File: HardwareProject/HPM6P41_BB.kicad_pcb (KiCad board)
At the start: 4 copper layers, 100 x 80.3 mm, 276 parts, among them J1 排针, J10 Conn_01x01, J11 Conn_01x01, J12 Conn_01x01, J13 排针, J14 排针, J2 USB_C_Receptacle_USB2.0_16P, J4 Conn_ARM_JTAG_SWD_20, J5 Conn_01x03, J6 Conn_01x03, J7 SMA, J8 SMA, J9 Conn_01x01, Q1 HYG080N10LS1C2, Q2 HYG080N10LS1C2, Q3 HYG080N10LS1C2, Q4 HYG080N10LS1C2, Q5 S8050, Q7 S8050, SW1 焊盘, SW2 Push_Button, SW3 Push_Button, SW4 Push_Button, U1 UCC27211ADRMR, U10 TJA1044GTK/3Z, U11 TPS54302, U12 LP5907MFX-3.3, U13 REF3030, U14 LM5164DDA, U15 SY8089, U16 INA241A3xDDF, U18 UCC27517, U2 UCC27211ADRMR, U20 SGM8551XN, U21 SGM8551XN, U22 TMP112xxDRL, U23 TPD4E05U06DQA, U24 CA-IS3762HN, U25 SYR838, U26 XC6206PxxxMR, U27 CA-IS3762HN, U28 TME-0505S, U3 UCC27517, U4 HPM6P41IPB1, U5 TPD4E05U06DQA, U6 AT24C08C-SSHM-T, U7 TMP112xxDRL, U8 TMP112xxDRL, U9 SIT3088ETK, Y1 24MHz ±10ppm 6pF

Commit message: 完成Rev4 电源 驱动 模拟 IO
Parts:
- removed R57: 1kΩ, Resistor_SMD:R_0603_1608Metric
- removed R75: 33Ω, Resistor_SMD:R_0603_1608Metric
- removed U21: SGM8551XN, Package_TO_SOT_SMD:TSOT-23-5
- added C104: SCC2211X102K502TG, kicad_community_lib:SCC2211X102K502T, F.Cu at (99.2, 123.5)
- added C105: SCC2211X102K502TG, kicad_community_lib:SCC2211X102K502T, B.Cu at (96.4, 102.9)
- added C98: 47pF,50V, Capacitor_SMD:C_0603_1608Metric, F.Cu at (184.2, 70.7)
- added R17: 10K, Resistor_SMD:R_0603_1608Metric, F.Cu at (129.2, 107.6)
- added R25: 10K, Resistor_SMD:R_0603_1608Metric, F.Cu at (129.2, 106.1)
- added R26: 10K, Resistor_SMD:R_0603_1608Metric, F.Cu at (143.2, 106.9)
- added R27: 100Ω, Resistor_SMD:R_0603_1608Metric, F.Cu at (185.0, 68.4)
- added R28: 100Ω, Resistor_SMD:R_0603_1608Metric, F.Cu at (183.5, 68.5)
- added R32: 1kΩ, Resistor_SMD:R_0603_1608Metric, F.Cu at (146.6, 76.6)
- added TP5: TestPoint_Probe, HPM6P41_BB:测试点, F.Cu at (126.1, 71.1)
- added TP6: TestPoint_Probe, HPM6P41_BB:测试点, F.Cu at (123.1, 71.1)
- added TP8: TestPoint_Probe, HPM6P41_BB:测试点, F.Cu at (131.3, 69.2)
- added U17: SGM8551XN, Package_TO_SOT_SMD:TSOT-23-5, F.Cu at (143.1, 76.6)
- C102, U24: moved to F.Cu
- C12, C13: value 1uF,100V -> 100nF 50V; footprint Capacitor_SMD:C_0805_2012Metric -> Capacitor_SMD:C_0603_1608Metric
- D1, D16, D17, D18, D19, D2, D3, D4, D5, D6, D7, D8: footprint Diode_SMD:D_SOD-323 -> Diode_SMD:D_SOD-523
- D13, D14: value BZT52C9V1S -> LM5Z12VT1G; footprint Diode_SMD:D_SOD-323 -> Diode_SMD:D_SOD-523
- J7, J8: footprint Connector_Coaxial:SMA_Amphenol_901-144_Vertical -> HPM6P41_BB:SMA_Amphenol_901-144_Vertical
- L1: value PQ26XX -> VER2923; footprint HPM6P41_BB:PQ26XX -> HPM6P41_BB:IND_VER2923_COC
- R56: value 1kΩ -> 0Ω
- R58: value 1kΩ -> 33Ω
- U28: footprint Converter_DCDC:Converter_DCDC_TRACO_TME_03xxS_05xxS_12xxS_Single_THT -> HPM6P41_BB:BXXXXS-1W隔离电源
- moved R64 180.7 mm to (157.9, 82.5), turned to 180 degrees
- moved R53 179.0 mm to (157.9, 85.0), turned to 180 degrees
- moved R52 177.4 mm to (157.9, 87.5), turned to 180 degrees
- moved R49 175.9 mm to (157.9, 90.0), turned to 180 degrees
- moved TP4 174.2 mm to (183.3, 91.7)
- moved TP3 174.2 mm to (183.3, 89.0)
- moved TP2 171.9 mm to (181.3, 90.2)
- moved TP1 171.8 mm to (181.3, 87.5)
- moved C7 153.8 mm to (134.6, 60.8)
- moved C19 153.6 mm to (115.3, 69.8), turned to -90 degrees
- moved C6 153.5 mm to (134.6, 59.3)
- moved C21 150.8 mm to (109.6, 69.8), turned to 90 degrees
- moved C11 150.2 mm to (130.8, 63.2), turned to -90 degrees
- moved R14 146.2 mm to (126.3, 56.4), turned to 180 degrees
- moved R60 145.9 mm to (132.3, 63.2), turned to -90 degrees
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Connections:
- net /MCU_MISC2/VTREF renamed VTREF
- C30 pad 1: ISO_GNDC -> Net-(J5-Pin_3)
- C30 pad 2: Net-(J5-Pin_3) -> ISO_GNDC
- C31 pad 1: Net-(J5-Pin_1) -> ISO_GNDC
- C31 pad 2: ISO_GNDC -> Net-(J5-Pin_1)
- C32 pad 1: ISO_GNDC -> Net-(J6-Pin_1)
- C32 pad 2: Net-(J6-Pin_1) -> ISO_GNDC
- C33 pad 1: Net-(J6-Pin_3) -> ISO_GNDC
- C33 pad 2: ISO_GNDC -> Net-(J6-Pin_3)
- C42 pad 2: GND -> GNDA
- C43 pad 2: GND -> GNDA
- C45 pad 2: GND -> GNDA
- C46 pad 2: GND -> GNDA
- C60 pad 2: GND -> GNDA
- C61 pad 2: GND -> GNDA
- C62 pad 1: Net-(U12-IN) -> Net-(U12-EN)
- C62 pad 2: GND -> GNDA
- C65 pad 2: GND -> GNDA
- C67 pad 2: GND -> GNDA
- C69 pad 2: GND -> GNDA
- C79 pad 2: GND -> GNDA
- C81 pad 2: GND -> GNDA
- C82 pad 2: GND -> GNDA
- C89 pad 2: GND -> GNDA
- C93 pad 2: GND -> GNDA
- C95 pad 2: GND -> GNDA
- C96 pad 2: GND -> GNDA
- C97 pad 2: GND -> GNDA
- C99 pad 2: GND -> GNDA
- D10 pad 1: Net-(J6-Pin_3) -> Net-(J6-Pin_1)
- D10 pad 2: Net-(J6-Pin_1) -> Net-(J6-Pin_3)
- D17 pad 2: GND -> GNDA
- D19 pad 2: GND -> GNDA
- D9 pad 1: Net-(J5-Pin_1) -> Net-(J5-Pin_3)
- D9 pad 2: Net-(J5-Pin_3) -> Net-(J5-Pin_1)
- FB5 pad 2: Net-(U12-IN) -> Net-(U12-EN)
- L1 pad 2: /BB/S1 -> /BB/S3
- L2 pad 3: Net-(J6-Pin_3) -> Net-(J6-Pin_1)
- L2 pad 4: Net-(J6-Pin_1) -> Net-(J6-Pin_3)
- L3 pad 3: Net-(J5-Pin_3) -> Net-(J5-Pin_1)
- L3 pad 4: Net-(J5-Pin_1) -> Net-(J5-Pin_3)
- R10 pad 1: /BB/S3 -> Net-(L1-Pad1)
- R10 pad 4: Net-(L1-Pad1) -> /BB/S1
- R56 pad 1: /BB/OutputVsense+ -> GNDA
- R56 pad 2: Net-(U21-+) -> GND
- R58 pad 2: Net-(R58-Pad2) -> /PD7
- R76 pad 1: Net-(R57-Pad2) -> Net-(U20--)
- TP7 pad 1: Net-(R73-Pad1) -> /PD9
- U12 pad 1: Net-(U12-IN) -> Net-(U12-EN)
- U12 pad 2: GND -> GNDA
- U12 pad 3: +5V -> Net-(U12-EN)
- U13 pad 3: GND -> GNDA
- U16 pad 1: /BB/ISENSE- -> Net-(U16--)
- U16 pad 2: GND -> GNDA
- U16 pad 3: GND -> GNDA
- U16 pad 4: GND -> GNDA
- U16 pad 8: /BB/ISENSE+ -> Net-(U16-+)
- U20 pad 1: Net-(R57-Pad2) -> Net-(U20--)
- U20 pad 2: GND -> GNDA
- U23 pad 2: /J_TCK -> /J_TDI
- U23 pad 4: /J_TDI -> /J_TCK
- U23 pad 7: /J_TDI -> /J_TCK
- U23 pad 9: /J_TCK -> /J_TDI
- U24 pad 14: /J_TMS -> /J_TCK
- U24 pad 15: /J_TCK -> /J_TMS
- U24 pad 2: /MCU_MISC2/CON_TCK -> /MCU_MISC2/CON_TMS
- U24 pad 3: /MCU_MISC2/CON_TMS -> /MCU_MISC2/CON_TCK
- U4 pad 38: GND -> GNDA
- U4 pad 39: GND -> GNDA
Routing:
- net +5VC: track 0.00 -> 40.5 mm, vias 0 -> 3
- net Net-(J6-Pin_1): track 0.00 -> 32.0 mm
- net Net-(J5-Pin_3): track 3.78 -> 33.9 mm
- net /MCU_MISC/CAN_STBY_ISO: track 0.00 -> 26.7 mm, vias 0 -> 2
- net ISO_GNDC: track 0.00 -> 24.5 mm, vias 0 -> 18
- net /MCU_MISC/CAN_RXD_ISO: track 0.00 -> 24.1 mm, vias 0 -> 2
- net /MCU_MISC/CAN_TXD_ISO: track 0.00 -> 23.6 mm, vias 0 -> 2
- net Net-(J6-Pin_3): track 0.00 -> 20.8 mm
- net Net-(J5-Pin_1): track 4.87 -> 21.6 mm
- net GNDA: track 0.00 -> 16.5 mm, vias 0 -> 2
- net VANA: track 0.00 -> 12.5 mm, vias 0 -> 17
- net /MCU_MISC/485_DE_ISO: track 0.00 -> 10.2 mm, vias 0 -> 2
- net +5V: track 8.57 -> 18.2 mm
- net /MCU_MISC/485_TX_ISO: track 0.00 -> 7.65 mm, vias 0 -> 2
- net GND: track 19.9 -> 27.5 mm, vias 10 -> 14
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- added copper zone on In1.Cu, net GND
- added copper zone on F.Cu, net GNDA
- added copper zone on B.Cu, net ISO_GNDC
- added copper zone on In1.Cu, net ISO_GNDC
- added copper zone on F.Cu, net VANA
- added copper zone on In2.Cu, net VANA

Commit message: 更新readme暂停通知，添加测试用例源代码
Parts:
- removed C105: SCC2211X102K502TG, kicad_community_lib:SCC2211X102K502T
- removed Q7: S8050, Package_TO_SOT_SMD:SOT-23
- removed R31, R44: 1k, Resistor_SMD:R_0603_1608Metric
- removed R71: 4.7k, Resistor_SMD:R_0603_1608Metric
- removed R72: 100Ω, Resistor_SMD:R_0603_1608Metric
- added C106: SCC1808X102K502TS, Capacitor_SMD:C_1808_4520Metric, F.Cu at (144.6, 104.9)
- added Q6: AO3400A, Package_TO_SOT_SMD:SOT-23, F.Cu at (212.9, 62.8)
- C104: value SCC2211X102K502TG -> SCC1808X102K502TS; footprint kicad_community_lib:SCC2211X102K502T -> Capacitor_SMD:C_1808_4520Metric
- Q5: value S8050 -> AO3400A
- moved R29 247.7 mm to (208.4, 45.9)
- moved R35 241.1 mm to (208.4, 48.5)
- moved R36 241.1 mm to (208.4, 51.0)
- moved R37 241.1 mm to (208.4, 53.5)
- moved C88 233.8 mm to (200.4, 61.0)
- moved C22 230.9 mm to (192.4, 61.0)
- moved C20 230.0 mm to (192.4, 58.5)
- moved U22 228.7 mm to (212.6, 52.2)
- moved U7 228.7 mm to (212.6, 46.2)
- moved U8 228.7 mm to (212.6, 49.2)
- moved C24 223.7 mm to (192.4, 63.5)
- moved C26 223.7 mm to (192.4, 66.0)
- moved R11 220.1 mm to (204.4, 53.5)
- moved R12 220.1 mm to (204.4, 56.0)
- moved R6 219.1 mm to (204.4, 48.5)
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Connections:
- C104 pad 1: ISO_GND -> ISO_GNDC
- C92 pad 1: +3.3V -> Net-(BZ1-+)
- Q5 pad 1: Net-(Q5-B) -> /PY3
- Q5 pad 3: Net-(Q5-C) -> Net-(BZ1--)
- R70 pad 1: +3.3V -> +5V
- S1 pad 11: Net-(Q5-C) -> Net-(Q6-D)
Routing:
- net USB_DN: track 5.80 -> 0.00 mm
- net USB_DP: track 4.61 -> 0.00 mm
- net ISO_GNDC: vias 18 -> 20
- net GND: vias 14 -> 17
- added copper zone on F.Cu, net ISO_GNDC

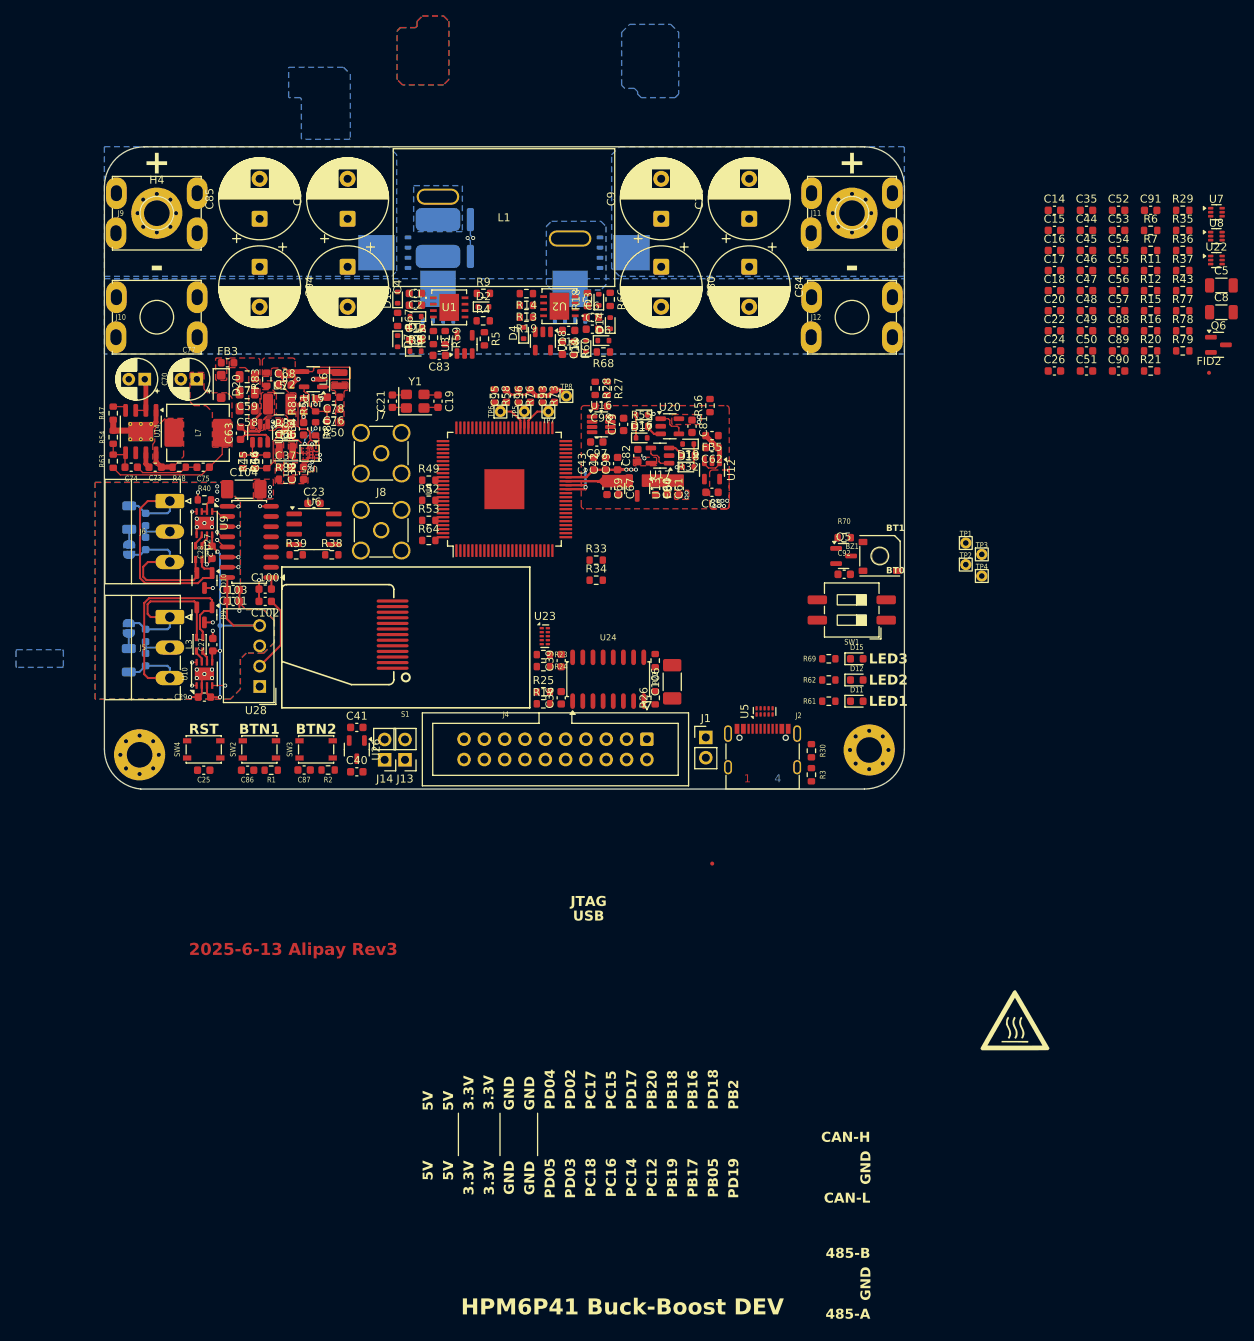
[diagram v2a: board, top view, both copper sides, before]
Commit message: rev4修改核心供电前保存（当前SYR838）
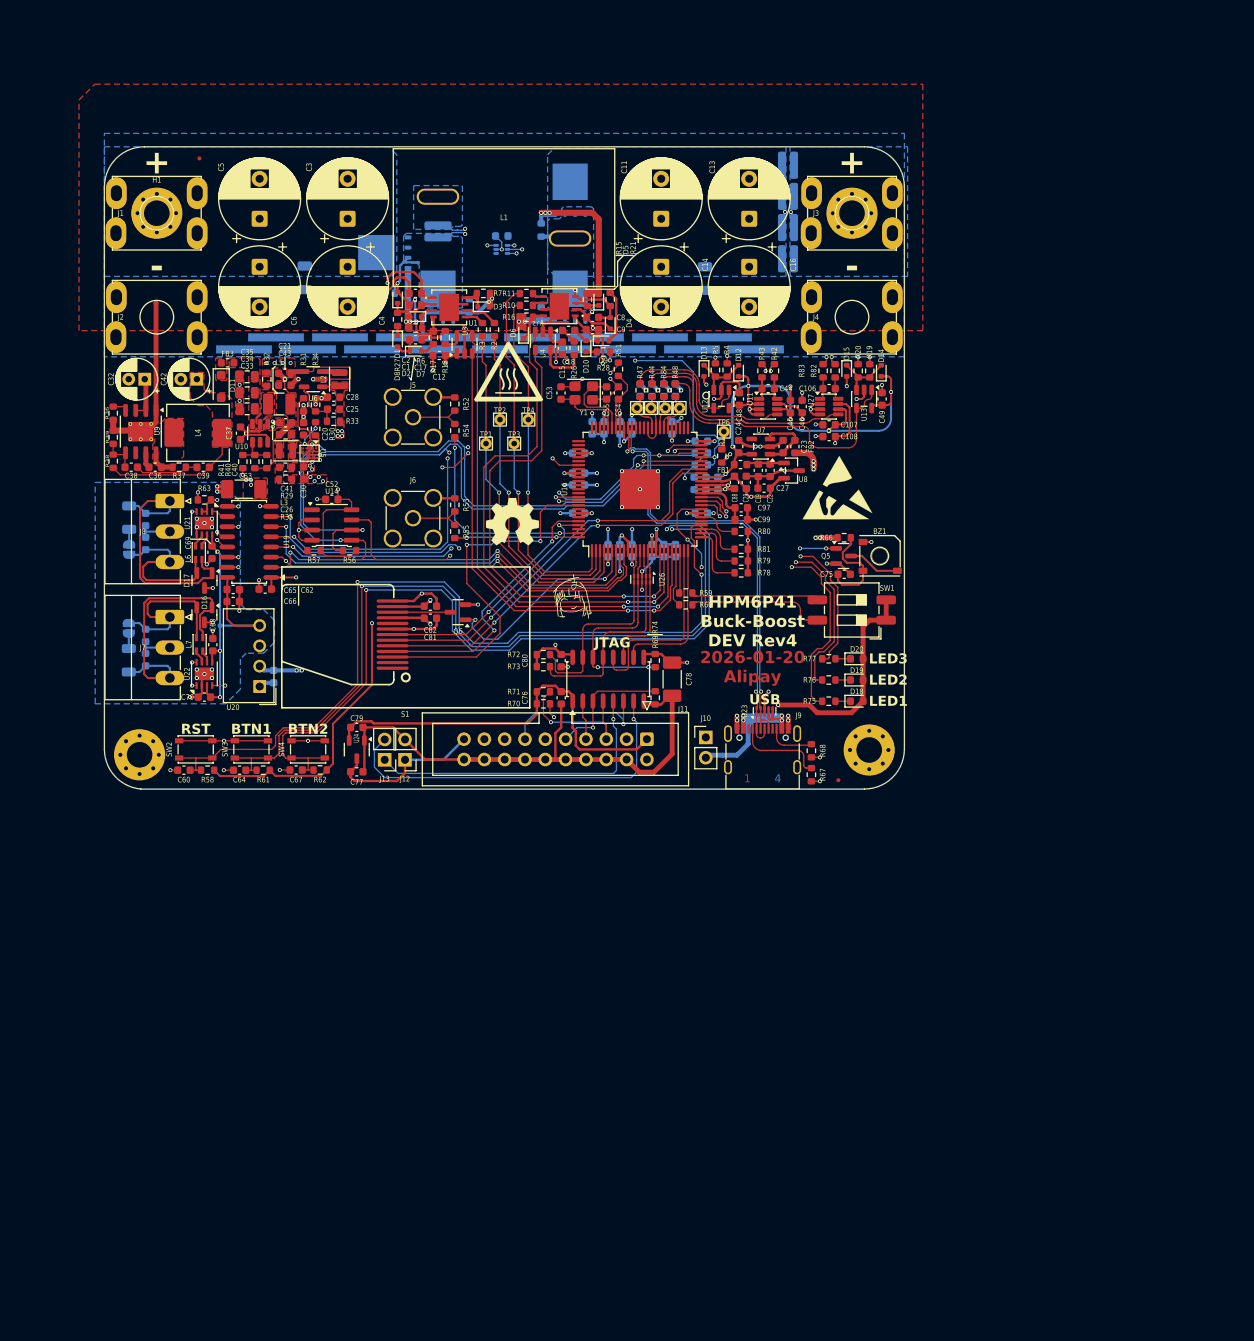
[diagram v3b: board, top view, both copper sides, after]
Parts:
- removed the C26 at (192.4, 66.0)
- removed the C42 at (136.2, 77.6)
- removed the C43 at (134.8, 77.6)
- removed the C60 at (142.5, 80.7)
- removed the C61 at (144.0, 80.7)
- removed the C62 at (149.5, 75.6)
- removed the C65 at (149.5, 81.2)
- removed the C67 at (137.9, 80.7)
- removed the C69 at (136.4, 80.7)
- removed the C79 at (138.5, 72.7)
- removed the C81 at (147.1, 72.9)
- removed the C82 at (140.3, 76.6)
- removed C89: 100nF,10V, Capacitor_SMD:C_0603_1608Metric
- removed the C97 at (135.2, 74.9)
- removed the C98 at (135.7, 70.5)
- removed the C99 at (137.8, 77.6)
- removed the D16 at (140.8, 71.5)
- removed the D17 at (140.8, 74.4)
- removed the D18 at (146.6, 78.0)
- removed the D19 at (146.6, 75.2)
- removed FB4, FB5: 100Ω@100MHz 2A, Inductor_SMD:L_0603_1608Metric
- removed the G*** at (187.4, 147.4)
- removed the R10 at (116.2, 49.4)
- removed the R27 at (136.4, 68.2)
- removed the R28 at (134.9, 68.2)
- removed the R32 at (146.6, 76.6)
- removed the R55 at (140.8, 73.0)
- removed the R56 at (149.3, 70.3)
- removed the TP6 at (123.1, 71.1)
- removed the U16 at (135.7, 72.7)
- removed U17: SGM8551XN, Package_TO_SOT_SMD:TSOT-23-5
- removed the U20 at (144.3, 72.9)
- removed the U22 at (212.6, 52.2)
- added C106: 47pF,50V, Capacitor_SMD:C_0603_1608Metric, F.Cu at (164.2, 68.2)
- added C107: 100nF,50V, Capacitor_SMD:C_0603_1608Metric, F.Cu at (164.2, 72.8)
- added C108: 100nF,50V, Capacitor_SMD:C_0603_1608Metric, F.Cu at (164.2, 74.2)
- added C109: 47pF,50V, Capacitor_SMD:C_0603_1608Metric, B.Cu at (143.5, 68.4)
- added C19: 22uF,10V, Capacitor_SMD:C_0603_1608Metric, F.Cu at (155.3, 78.5)
- added C22: 100nF,50V, Capacitor_SMD:C_0603_1608Metric, F.Cu at (156.8, 78.5)
- added C23: 1uF,10V, Capacitor_SMD:C_0603_1608Metric, F.Cu at (158.4, 75.5)
- added C24: 1uF,10V, Capacitor_SMD:C_0603_1608Metric, F.Cu at (152.9, 75.5)
- added C27: 4.7uF,10V, Capacitor_SMD:C_0603_1608Metric, F.Cu at (156.1, 80.7)
- added C29: 100nF,50V, Capacitor_SMD:C_0603_1608Metric, F.Cu at (153.8, 80.0)
- added C44: 47pF,50V, Capacitor_SMD:C_0603_1608Metric, F.Cu at (156.6, 68.2)
- added C48: 100nF,50V, Capacitor_SMD:C_0603_1608Metric, F.Cu at (153.0, 69.5)
- added C49: 100nF,50V, Capacitor_SMD:C_0603_1608Metric, F.Cu at (170.8, 69.5)
- added C84: 22uF,10V, Capacitor_SMD:C_0603_1608Metric, B.Cu at (147.3, 80.1)
- added C85: 4.7uF,10V, Capacitor_SMD:C_0603_1608Metric, B.Cu at (148.8, 80.1)
- added C86: 100nF,50V, Capacitor_SMD:C_0603_1608Metric, B.Cu at (150.3, 80.1)
- added D12: 1N4148WS, Diode_SMD:D_SOD-523, F.Cu at (152.9, 66.0)
- added D13: 1N4148WS, Diode_SMD:D_SOD-523, F.Cu at (148.6, 66.0)
- added D14: 1N4148WS, Diode_SMD:D_SOD-523, F.Cu at (170.7, 66.0)
- added D15: 1N4148WS, Diode_SMD:D_SOD-523, F.Cu at (166.4, 66.0)
- added FB1: 100Ω@100MHz 2A, Inductor_SMD:L_0603_1608Metric, F.Cu at (153.1, 77.7)
- added FB2: 100Ω@100MHz 2A, Inductor_SMD:L_0603_1608Metric, F.Cu at (159.9, 75.5)
- added G***: LOGO, LOGO, F.Cu at (131.9, 94.4)
- added G***: LOGO, LOGO, F.Cu at (124.1, 66.3)
- added G***: LOGO, LOGO, B.Cu at (128.1, 94.6)
- added G***: LOGO, LOGO, B.Cu at (105.9, 93.5)
- added R1: 0Ω, Resistor_SMD:R_0603_1608Metric, F.Cu at (150.8, 76.7)
- added R12: 1mΩ 1W, Resistor_SMD:R_0612_1632Metric, B.Cu at (115.3, 48.6)
- added R22: 1mΩ 1W, Resistor_SMD:R_0612_1632Metric, B.Cu at (159.1, 40.3)
- added R23: 1mΩ 1W, Resistor_SMD:R_0612_1632Metric, B.Cu at (159.1, 44.2)
- added R24: 1mΩ 1W, Resistor_SMD:R_0612_1632Metric, B.Cu at (159.1, 48.1)
- added R25: 1mΩ 1W, Resistor_SMD:R_0612_1632Metric, B.Cu at (159.1, 52.0)
- added R42: 100Ω, Resistor_SMD:R_0603_1608Metric, F.Cu at (157.3, 66.0)
- added R43: 100Ω, Resistor_SMD:R_0603_1608Metric, F.Cu at (155.8, 66.0)
- added R82: 100Ω, Resistor_SMD:R_0603_1608Metric, F.Cu at (164.9, 66.0)
- added R83: 100Ω, Resistor_SMD:R_0603_1608Metric, F.Cu at (163.4, 66.0)
- added R84: 33Ω, Resistor_SMD:R_0603_1608Metric, F.Cu at (143.5, 68.4)
- added REF**: 7x1mm_导流条, 1MyFootPrint:7x1mm_导流条, B.Cu at (95.0, 61.8)
- added REF**: 7x1mm_导流条, 1MyFootPrint:7x1mm_导流条, B.Cu at (135.1, 61.8)
- added REF**: 7x1mm_导流条, 1MyFootPrint:7x1mm_导流条, B.Cu at (107.0, 63.3)
- added REF**: 7x1mm_导流条, 1MyFootPrint:7x1mm_导流条, B.Cu at (147.1, 63.3)
- added REF**: 7x1mm_导流条, 1MyFootPrint:7x1mm_导流条, B.Cu at (139.1, 63.3)
- added REF**: 7x1mm_导流条, 1MyFootPrint:7x1mm_导流条, B.Cu at (115.0, 63.3)
- added REF**: 7x1mm_导流条, 1MyFootPrint:7x1mm_导流条, B.Cu at (111.0, 61.8)
- added REF**: 7x1mm_导流条, 1MyFootPrint:7x1mm_导流条, B.Cu at (91.0, 63.3)
- added REF**: 7x1mm_导流条, 1MyFootPrint:7x1mm_导流条, B.Cu at (151.1, 61.8)
- added REF**: 7x1mm_导流条, 1MyFootPrint:7x1mm_导流条, B.Cu at (103.0, 61.8)
- added REF**: OSHW-Symbol_6.7x6mm_SilkScreen, Symbol:OSHW-Symbol_6.7x6mm_SilkScreen, F.Cu at (124.6, 84.9)
- added REF**: 7x1mm_导流条, 1MyFootPrint:7x1mm_导流条, B.Cu at (143.1, 61.8)
- added REF**: ESD-Logo_8.9x8mm_SilkScreen, Symbol:ESD-Logo_8.9x8mm_SilkScreen, F.Cu at (165.2, 80.6)
- added REF**: 7x1mm_导流条, 1MyFootPrint:7x1mm_导流条, B.Cu at (99.0, 63.3)
- added REF**: 7x1mm_导流条, 1MyFootPrint:7x1mm_导流条, B.Cu at (155.1, 63.3)
- added REF**: 7x1mm_导流条, 1MyFootPrint:7x1mm_导流条, B.Cu at (131.1, 63.3)
- added REF**: 7x1mm_导流条, 1MyFootPrint:7x1mm_导流条, B.Cu at (119.0, 61.8)
- added REF**: 7x1mm_导流条, 1MyFootPrint:7x1mm_导流条, B.Cu at (127.0, 61.8)
- added REF**: 7x1mm_导流条, 1MyFootPrint:7x1mm_导流条, B.Cu at (123.0, 63.3)
- added TP8: TestPoint_Probe, HPM6P41_BB:测试点, F.Cu at (145.5, 70.7)
- added TP9: TestPoint_Probe, HPM6P41_BB:测试点, F.Cu at (140.2, 70.7)
- added U11: INA241A3xDDF, Package_TO_SOT_SMD:SOT-23-8, F.Cu at (156.6, 70.5)
- added U27: INA241A3xDDF, Package_TO_SOT_SMD:SOT-23-8, F.Cu at (164.2, 70.5)
- added U7: LP5907MFX-3.3, Package_TO_SOT_SMD:SOT-23-5, F.Cu at (155.7, 75.5)
- C1, C2: value 100nF 50V -> 100nF,50V
- C10: renamed from C8; moved to B.Cu
- C100: renamed from C57; moved to B.Cu
- C101: renamed from C14; value 100nF,10V -> 100nF,50V; moved to B.Cu
- C102: renamed from C15; value 100nF,10V -> 100nF,50V; moved to B.Cu
- C103: renamed from C16; value 100nF,10V -> 100nF,50V; moved to B.Cu
- C104: renamed from C17; value 100nF,10V -> 100nF,50V; moved to B.Cu
- C105: renamed from C18; value 100nF,10V -> 100nF,50V; moved to B.Cu
- C17: renamed from C12; value 100nF 50V -> 100nF,50V
- C18: renamed from C13; value 100nF 50V -> 100nF,50V
- C37: renamed from C63; value 100nF -> 100nF,50V
- C45: value 10nF,10V -> 100nF,50V
- C46: value 4.7uF,10V -> 100nF,50V
- C47: renamed from C93; moved to B.Cu
- C50: renamed from C96; moved to B.Cu
- C51: renamed from C95; moved to B.Cu
- C52: renamed from C23; value 100nF -> 100nF,50V
- C54: renamed from C20; value 100nF,10V -> 100nF,50V
- C56: renamed from C22; value 100nF,10V -> 100nF,50V; moved to B.Cu
- C57: renamed from C24; value 100nF -> 100nF,50V; moved to B.Cu
- C60: renamed from C25; value 100nF -> 100nF,50V
- C61: renamed from C102; moved to B.Cu
- C62: renamed from C100; value 100nF -> 100nF,50V
- C64: renamed from C86; value 100nF -> 100nF,50V
- C65: renamed from C101; value 100nF -> 100nF,50V
- C67: renamed from C87; value 100nF -> 100nF,50V
- C68: renamed from C27; value 100nF -> 100nF,50V
- C69: renamed from C28; value 100nF -> 100nF,50V
- C7: renamed from C5; moved to B.Cu
- C70: renamed from C29; value 100nF -> 100nF,50V
- C76: renamed from C36; value 100nF -> 100nF,50V
- C8: renamed from C6; value 100nF 50V -> 100nF,50V
- C80: renamed from C39; value 100nF -> 100nF,50V
- C81: renamed from C90; value 100nF,10V -> 100nF,50V
- C82: renamed from C91; value 100nF,10V -> 100nF,50V
- C83: renamed from C35; value 100nF,10V -> 100nF,50V; moved to B.Cu
- C87: renamed from C44; moved to B.Cu
- C88: value 100nF -> 10nF,10V
- C9: renamed from C7; value 100nF 50V -> 100nF,50V
- C90: renamed from C47; moved to B.Cu
- C91: renamed from C48; moved to B.Cu
- C92: renamed from C49; moved to B.Cu
- C93: renamed from C50; moved to B.Cu
- C94: renamed from C51; moved to B.Cu
- C95: renamed from C52; value 100nF,10V -> 100nF,50V; moved to B.Cu
- C96: renamed from C53; moved to B.Cu
- C98: renamed from C55; moved to B.Cu
- C99: renamed from C56; value 100nF,10V -> 100nF,50V
- R13: renamed from R15; moved to B.Cu
- R14: renamed from R16; moved to B.Cu
- R49: renamed from R35; moved to B.Cu
- R50: renamed from R36; moved to B.Cu
- R8: renamed from R11; moved to B.Cu
- R9: renamed from R12; moved to B.Cu
- U12: value LP5907MFX-3.3 -> SGM8551XN; footprint Package_TO_SOT_SMD:SOT-23-5 -> Package_TO_SOT_SMD:TSOT-23-5
- U13: value REF3030 -> SGM8551XN; footprint Package_TO_SOT_SMD:SOT-23 -> Package_TO_SOT_SMD:TSOT-23-5
- U15: renamed from U7; moved to B.Cu
- U8: value TMP112xxDRL -> REF3030; footprint Package_TO_SOT_SMD:SOT-563 -> Package_TO_SOT_SMD:SOT-23
- moved R58 137.0 mm to (86.5, 115.9), turned to 180 degrees
- moved C7 114.6 mm to (98.7, 54.4), turned to -90 degrees
- moved FID1 109.0 mm to (85.5, 39.5)
- moved C82 102.7 mm to (114.3, 95.4)
- moved Q6 100.8 mm to (117.8, 96.2), turned to 180 degrees
- moved R8 93.7 mm to (110.7, 56.3)
- moved C81 91.4 mm to (114.3, 96.9)
- moved U15 89.4 mm to (123.3, 50.8), turned to 180 degrees
- moved R9 85.2 mm to (119.2, 57.9), turned to -90 degrees
- moved R13 76.9 mm to (128.2, 48.4), turned to 90 degrees
- moved R14 76.2 mm to (128.2, 58.9), turned to -90 degrees
- moved C96 74.0 mm to (132.9, 78.8)
- moved R51 73.3 mm to (137.8, 65.8), turned to 90 degrees
- moved C87 72.0 mm to (136.6, 88.5), turned to 90 degrees
- moved C100 70.9 mm to (132.9, 80.3)
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- renumbered C9 to C11, C83 to C12, C10 to C13, C80 to C14, C11 to C15, C84 to C16, C34 to C20, C72 to C21, C76 to C25, C37 to C26, C78 to C28, C38 to C30, C70 to C32, C58 to C33, C59 to C34, C71 to C35, C73 to C36, C74 to C38, C75 to C39, C64 to C40, C66 to C41, C77 to C42, C68 to C43, C85 to C5, C19 to C53, C21 to C55, C94 to C6, C104 to C63, C103 to C66, C31 to C71, C30 to C72, C33 to C73, C32 to C74, C92 to C75, C40 to C77, C106 to C78, C41 to C79, C54 to C97, D13 to D1, D8 to D10, D20 to D11, D9 to D16, D10 to D17, D11 to D18, D12 to D19, D1 to D2, D15 to D20, D2 to D3, D14 to D4, D3 to D5, D4 to D6, D5 to D7, D7 to D8, D6 to D9, H4 to H1, H3 to H2, H2 to H3, H1 to H4, J9 to J1, J1 to J10, J4 to J11, J13 to J12, J14 to J13, J10 to J2, J11 to J3, J12 to J4, J7 to J5, J8 to J6, J5 to J7, J6 to J8, J2 to J9, L6 to L2, L8 to L3, L7 to L4, L2 to L6, L3 to L7, R13 to R10, R14 to R11, R18 to R15, R19 to R16, R65 to R17, R59 to R18, R20 to R19, R4 to R2, R21 to R20, R66 to R21, R60 to R26, R67 to R27, R68 to R28, R84 to R29, R5 to R3, R80 to R30, R81 to R31, R83 to R32, R50 to R33, R51 to R34, R82 to R35, R47 to R36, R48 to R37, R63 to R38, R54 to R39, R6 to R4, R45 to R40, R46 to R41, R73 to R44, R76 to R47, R58 to R48, R7 to R5, R29 to R51, R53 to R52, R64 to R53, R49 to R54, R52 to R55, R38 to R56, R39 to R57, R37 to R58, R33 to R59, R8 to R6, R34 to R60, R1 to R61, R2 to R62, R40 to R63, R41 to R64, R42 to R65, R70 to R66, R3 to R67, R30 to R68, R26 to R69, R9 to R7, R17 to R70, R25 to R71, R23 to R72, R24 to R73, R22 to R74, R61 to R75, R62 to R76, R69 to R77, R43 to R78, R77 to R79, R78 to R80, R79 to R81, SW4 to SW2, SW2 to SW3, SW3 to SW4, TP3 to TP1, TP4 to TP2, TP1 to TP3, TP2 to TP4, TP8 to TP6, U11 to U10, U6 to U14, U4 to U16, U27 to U19, U28 to U20, U9 to U21, U10 to U22, U5 to U23, U26 to U24, U24 to U25, U23 to U26, U18 to U4, U25 to U5, U15 to U6, U14 to U9
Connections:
- net /BB/S1 renamed /ISENSE+
- C10 pad 1: VOUT -> /BB/ISENSE2+
- C11 pad 1: VOUT -> /BB/ISENSE2+
- C13 pad 1: VOUT -> /BB/ISENSE2+
- C14 pad 1: VOUT -> /BB/ISENSE2+
- C16 pad 1: VOUT -> /BB/ISENSE2+
- C21 pad 1: Net-(U15-EN) -> +5V
- C26 pad 1: Net-(U25-VOUT) -> Net-(C26-Pad1)
- C40 pad 1: +5V -> 5V_OUT
- C41 pad 1: +5V -> 5V_OUT
- C43 pad 1: +5V -> 5V_OUT
- C45 pad 1: VREFH -> VANA
- C47 pad 1: /PD9 -> /PD5
- C50 pad 1: /PD8 -> /PD6
- C51 pad 1: /PD7 -> /PD10
- C88 pad 1: GND -> VREFH
- C88 pad 2: +3.3V -> GNDA
- L1 pad 1: Net-(L1-Pad1) -> /ISENSE-
- L3 pad 1: Net-(U25-VOUT) -> Net-(C26-Pad1)
- L5 pad 2: +5V -> 5V_OUT
- Q3 pad 5: VOUT -> /BB/ISENSE2+
- Q6 pad 1: /PA0 -> /PA11
- R29 pad 1: +5V -> 5V_OUT
- R32 pad 1: +5V -> 5V_OUT
- R32 pad 2: Net-(U15-EN) -> +5V
- R35 pad 1: Net-(U25-VOUT) -> Net-(C26-Pad1)
- R40 pad 1: +5V -> 5V_OUT
- R44 pad 2: /PD9 -> /PD5
- R47 pad 1: Net-(U20--) -> Net-(U12--)
- R47 pad 2: /PD8 -> /PD6
- R48 pad 1: Net-(U17--) -> Net-(U13--)
- R48 pad 2: /PD7 -> /PD10
- TP5 pad 1: /PD8 -> /PD5
- TP7 pad 1: /PD9 -> /PD8
- U12 pad 1: Net-(U12-EN) -> Net-(U12--)
- U12 pad 3: Net-(U12-EN) -> /BB/InputVsense+
- U12 pad 4: unconnected-(U12-NC-Pad4) -> Net-(U12--)
- U13 pad 1: Net-(U13-IN) -> Net-(U13--)
- U13 pad 2: VREFH -> GNDA
- U13 pad 3: GNDA -> /BB/OutputVsense+
- U16 pad 57: /PD9 -> /PD10
- U16 pad 59: /PD7 -> /PD5
- U23 pad 4: +5V -> VBUS
- U23 pad 5: +5V -> VBUS
- U23 pad 6: +5V -> VBUS
- U23 pad 7: +5V -> VBUS
- U25 pad 10: /MCU_MISC2/ISO_TX -> /PA0
- U25 pad 12: /MCU_MISC2/ISO_RX -> /PA1
- U5 pad A4: Net-(U25-VOUT) -> VDD_SOC
- U6 pad 1: Net-(U15-EN) -> +5V
- U6 pad 4: Net-(U15-EN) -> +5V
- U8 pad 1: /PD24 -> Net-(U8-IN)
- U8 pad 2: GND -> VREFH
- U8 pad 3: /PD23 -> GNDA
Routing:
- net GND: track 27.5 -> 260.2 mm, vias 17 -> 73
- net +3.3V: track 1.47 -> 197.4 mm, vias 0 -> 22
- net /PD24: track 0.50 -> 151.0 mm, vias 1 -> 5
- net /PD25: track 0.54 -> 148.1 mm, vias 1 -> 5
- net /PD20: track 0.00 -> 116.4 mm, vias 0 -> 3
- net /PD21: track 0.00 -> 114.3 mm, vias 0 -> 3
- net /MCU_MISC/RESETN: track 0.00 -> 105.8 mm, vias 0 -> 2
- net VIN: track 5.23 -> 104.2 mm, vias 0 -> 1
- net /ISENSE+: track 0.00 -> 94.9 mm, vias 0 -> 5
- net Vdrv: track 17.8 -> 105.0 mm, vias 0 -> 4
- net /ISENSE-: track 0.00 -> 73.5 mm, vias 0 -> 2
- net ISO_GND: track 0.00 -> 66.1 mm
- net /PA18: track 0.00 -> 65.2 mm, vias 0 -> 2
- net /PD22: track 0.00 -> 63.5 mm, vias 0 -> 4
- net /PA17: track 0.00 -> 61.4 mm, vias 0 -> 2
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- added copper zone on In2.Cu, net +3.3V
- added copper zone on In2.Cu, net +5V
- added copper zone on B.Cu, net /BB/ISENSE2+
- added copper zone on B.Cu, net /ISENSE-
- added copper zone on F.Cu, net 5V_OUT
- added copper zone on In2.Cu, net GNDA
- added copper zone on In1.Cu, net ISO_GND
- added copper zone on In2.Cu, net ISO_GND
- added copper zone on F.Cu, net Net-(C26-Pad1)
- added copper zone on In2.Cu, net VDD_SOC
- removed copper zone on F.Cu, net GNDA
- removed copper zone on F.Cu, net ISO_GNDC
- removed copper zone on B.Cu, net Net-(L1-Pad1)
- removed copper zone on F.Cu, net Net-(U15-EN)
- removed copper zone on F.Cu, net Net-(U25-VOUT)
- removed copper zone on F.Cu, net VANA
- removed copper zone on In2.Cu, net VANA
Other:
- board text added: "2026-01-20 Alipay"
- board text added: "HPM6P41 Buck-Boost DEV Rev4"
- board text added: "Rev4 Designed by Alipay@ 4-Switch Buck-Boost Converter"
- board text added: "https://github.com/Alipay1/HPM6P41_BB"
- board text removed: "2025-6-13 Alipay Rev3"
- board text removed: "3.3V"
- board text removed: "5V"
- board text removed: "BT0"
- board text removed: "BT1"
- board text removed: "HPM6P41 Buck-Boost DEV"
- board text removed: "PB05"
- board text removed: "PB16"
- board text removed: "PB17"
- board text removed: "PB18"
- board text removed: "PB19"
- board text removed: "PB2"
- board text removed: "PB20"
- board text removed: "PC12"
- board text removed: "PC14"
- board text removed: "PC15"
- board text removed: "PC16"
- board text removed: "PC17"
- board text removed: "PC18"
- board text removed: "PD02"
- board text removed: "PD03"
- board text removed: "PD04"
- board text removed: "PD05"
- board text removed: "PD17"
- board text removed: "PD18"
- board text removed: "PD19"
